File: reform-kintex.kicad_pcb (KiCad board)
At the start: 8 copper layers, 68 x 67.8 mm, 345 parts, among them J1 Conn_01x33, J2 JTAG_01x06, J3 Conn_01x03_Male, U1 MNT Reform 2.0 SoM Socket, U10 W25Q128JVS, U11 TPS62823DLC, U12 TPS62823DLC, U13 TPS62823DLC, U14 TPS62823DLC, U15 TPS62823DLC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

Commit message: more routing (39)
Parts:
- C82, C83: moved to F.Cu
- R26, R53: moved to B.Cu
- moved TP5 16.5 mm to (114.8, 147.9)
- moved C97 14.2 mm to (132.7, 105.7), turned to 180 degrees
- moved FB2 11.7 mm to (132.9, 107.0), turned to 180 degrees
- moved C93 10.2 mm to (141.7, 110.7), turned to 270 degrees
- moved FB1 9.35 mm to (143.3, 109.2), turned to 270 degrees
- moved C89 7.90 mm to (144.7, 109.8)
- moved R56 7.72 mm to (164.9, 125.5), turned to 180 degrees
- moved R50 6.37 mm to (151.2, 163.5), turned to 90 degrees
- moved C87 5.92 mm to (133.3, 102.5), turned to 180 degrees
- moved R53 5.33 mm to (161.3, 142.1), turned to 180 degrees
- moved C22 5.15 mm to (150.8, 162.0), turned to 180 degrees
- moved R51 5.06 mm to (152.8, 161.8)
- moved C94 4.97 mm to (143.4, 107.2), turned to 180 degrees
- moved C90 4.55 mm to (137.6, 102.5)
- moved C98 4.49 mm to (139.5, 105.3), turned to 0 degrees
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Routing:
- net GND: track 712.9 -> 942.5 mm, vias 287 -> 341
- net +3V3: track 227.7 -> 412.4 mm, vias 23 -> 33
- net EN_VDDR: track 0.00 -> 124.0 mm, vias 0 -> 4
- net +1V2: track 136.1 -> 257.2 mm, vias 24 -> 31
- net +5V: track 159.7 -> 198.4 mm, vias 8 -> 14
- net VTTREF: track 83.0 -> 117.2 mm, vias 10 -> 15
- net EN_VIO: track 56.5 -> 83.5 mm, vias 3 -> 4
- net +1V1: track 96.5 -> 121.6 mm, vias 26 -> 29
- net ETH_VDDL: track 0.00 -> 21.6 mm, vias 0 -> 2
- net Vtt: track 32.6 -> 53.8 mm, vias 0 -> 6
- net QSPI_DQ2: track 2.50 -> 23.4 mm, vias 1 -> 2
- net DSI_RST_N: track 2.73 -> 23.6 mm, vias 2 -> 3
- net HDMI_SDA: track 28.3 -> 48.6 mm
- net HDMI_SCL: track 28.6 -> 48.6 mm
- net EN_VAUX: track 0.00 -> 19.7 mm, vias 0 -> 2
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- added copper zone on GND2.Cu, net GND
- added copper zone on GND3.Cu, net GND

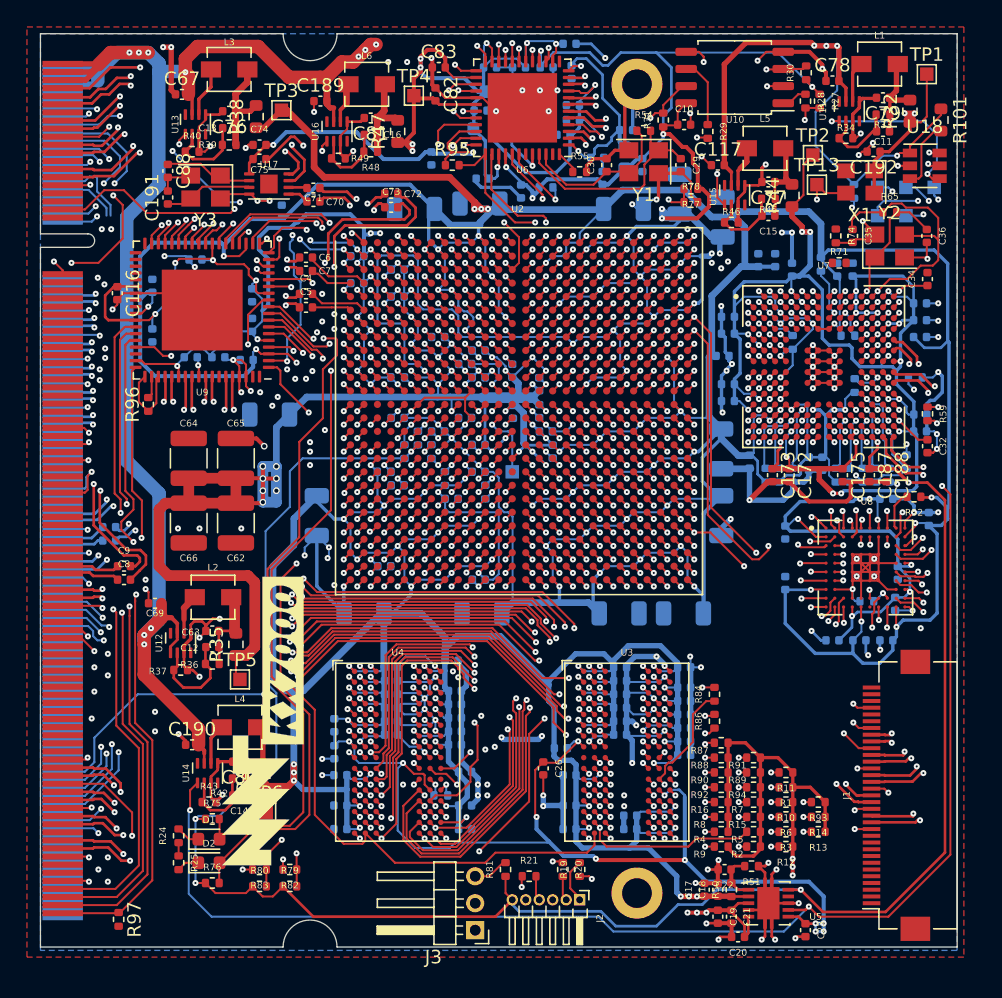
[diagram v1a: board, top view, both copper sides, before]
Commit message: fully routed
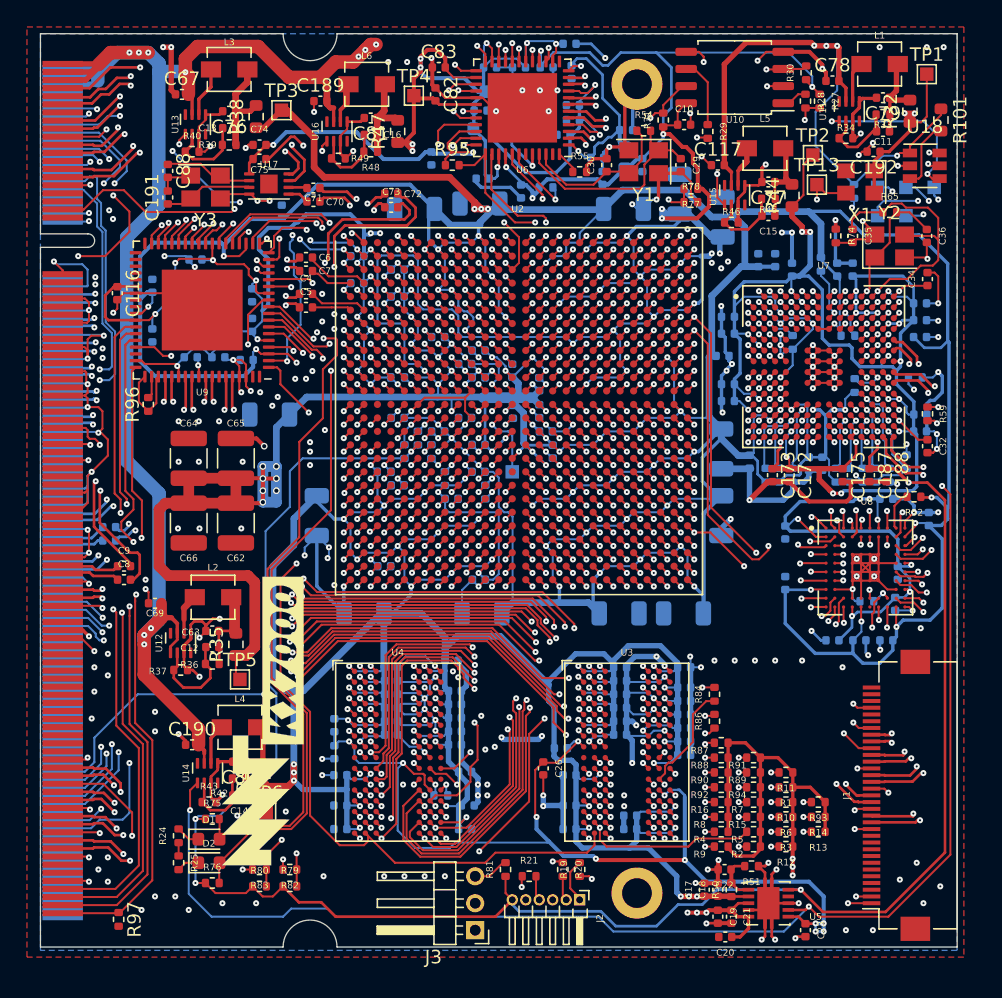
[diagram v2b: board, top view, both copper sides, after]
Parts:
- removed R71: 0, Resistor_SMD:R_0402_1005Metric
- moved C20 0.95 mm to (150.8, 167.0)
- moved C164 0.20 mm to (131.7, 157.2)
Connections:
- U1 pad 13: GND -> Net-(U1-Pad13)
- U1 pad 25: GND -> Net-(U1-Pad25)
- U2 pad G16: UART3_TX -> UART3_RX
- U2 pad H16: UART3_RX -> UART3_TX
- U2 pad Y23: Net-(U2-PadY23) -> TUSB_CLKOUT
- U7 pad D10: Net-(R71-Pad1) -> TUSB_CLKOUT
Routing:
- net GND: track 942.5 -> 1095.8 mm, vias 341 -> 380
- net TUSB_CLKOUT: track 0.00 -> 27.2 mm, vias 0 -> 2
- net UART3_RX: track 44.7 -> 57.7 mm
- net UART3_TX: track 47.1 -> 59.4 mm
- net +1V8: track 455.5 -> 460.3 mm
- net Net-(R71-Pad1): track 4.80 -> 0.00 mm, vias 1 -> 0
- net (no net): track 3.96 -> 0.00 mm, vias 7 -> 0
- net /RAM/USB2_GTX_P: track 44.0 -> 42.7 mm
- net ETH0_LED_LINK1: track 63.5 -> 64.5 mm
- net ETH0_LED_RX: track 76.1 -> 77.0 mm
- net USB2_RX_N: track 54.2 -> 53.4 mm
- net EDP_IRQ: track 2.71 -> 1.97 mm
- net EDP_RESETn: track 2.67 -> 1.97 mm
- net Net-(U2-PadY23): track 0.71 -> 0.00 mm, vias 1 -> 0
- net USB2_RX_P: track 55.9 -> 55.2 mm
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
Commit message: connect some missing i2c signals, backlight_en
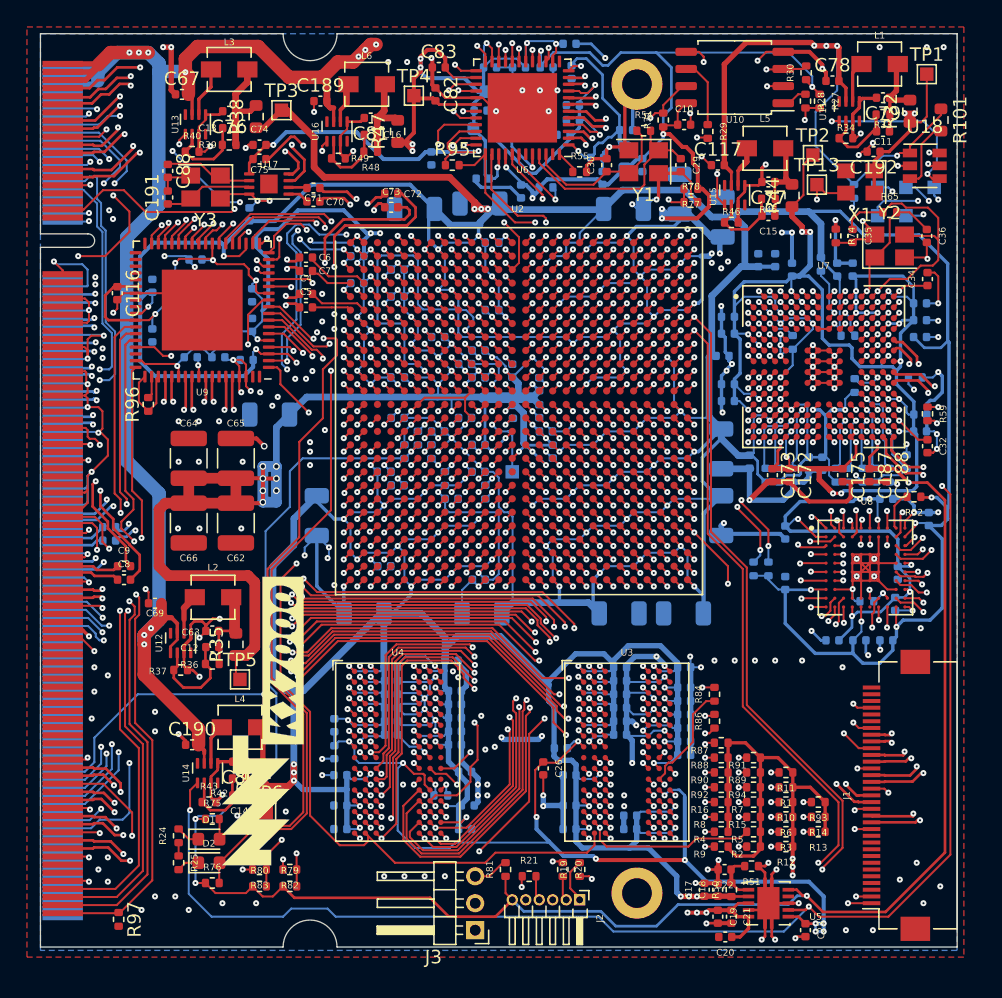
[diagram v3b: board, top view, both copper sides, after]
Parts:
- added R102: 4k7, Resistor_SMD:R_0402_1005Metric, B.Cu at (133.5, 120.5)
- added R103: 4k7, Resistor_SMD:R_0402_1005Metric, B.Cu at (154.0, 139.7)
- added R104: 4k7, Resistor_SMD:R_0402_1005Metric, B.Cu at (152.9, 139.7)
- added R71: 4k7, Resistor_SMD:R_0402_1005Metric, B.Cu at (133.5, 115.5)
- moved C118 2.41 mm to (115.5, 113.4)
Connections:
- net Net-(U8-PadK6) renamed DSI_REFCLK
- U1 pad 104: GND -> Net-(U1-Pad104)
- U2 pad B16: Net-(U2-PadB16) -> BACKLIGHT_EN
- U2 pad G26: I2C1_SCL -> DAC_SDA
- U2 pad H26: I2C1_SDA -> DAC_SCL
- U2 pad W26: Net-(U2-PadW26) -> DISP2_SDA
- U2 pad Y26: Net-(U2-PadY26) -> DISP2_SCL
- U8 pad A8: I2C1_SCL -> DISP2_SCL
- U8 pad B8: I2C1_SDA -> DISP2_SDA
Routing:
- net DAC_SDA: track 0.00 -> 124.2 mm, vias 0 -> 3
- net DAC_SCL: track 0.00 -> 121.6 mm, vias 0 -> 3
- net BACKLIGHT_EN: track 0.00 -> 55.6 mm, vias 0 -> 4
- net I2C1_SCL: track 33.4 -> 0.00 mm, vias 3 -> 0
- net I2C1_SDA: track 31.6 -> 0.00 mm, vias 3 -> 0
- net DISP2_SCL: track 0.00 -> 21.7 mm, vias 0 -> 4
- net DISP2_SDA: track 0.00 -> 20.3 mm, vias 0 -> 4
- net +1V8: track 460.3 -> 463.3 mm
- net TUSB_TX_D1: track 11.1 -> 8.20 mm
- net /RAM/PCIE2_GTX_CLK_HOST_P: track 14.2 -> 11.6 mm
- net TUSB_TX_DATAK1: track 21.2 -> 23.1 mm
- net DSI_RST_N: track 23.6 -> 25.3 mm
- net TUSB_TX_D0: track 12.8 -> 11.3 mm
- net DISP1_SDA: track 29.2 -> 30.4 mm
- net TUSB_CLKOUT: track 27.2 -> 26.1 mm
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
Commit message: silkscreen cleanup, 3d models, some footprint fixes
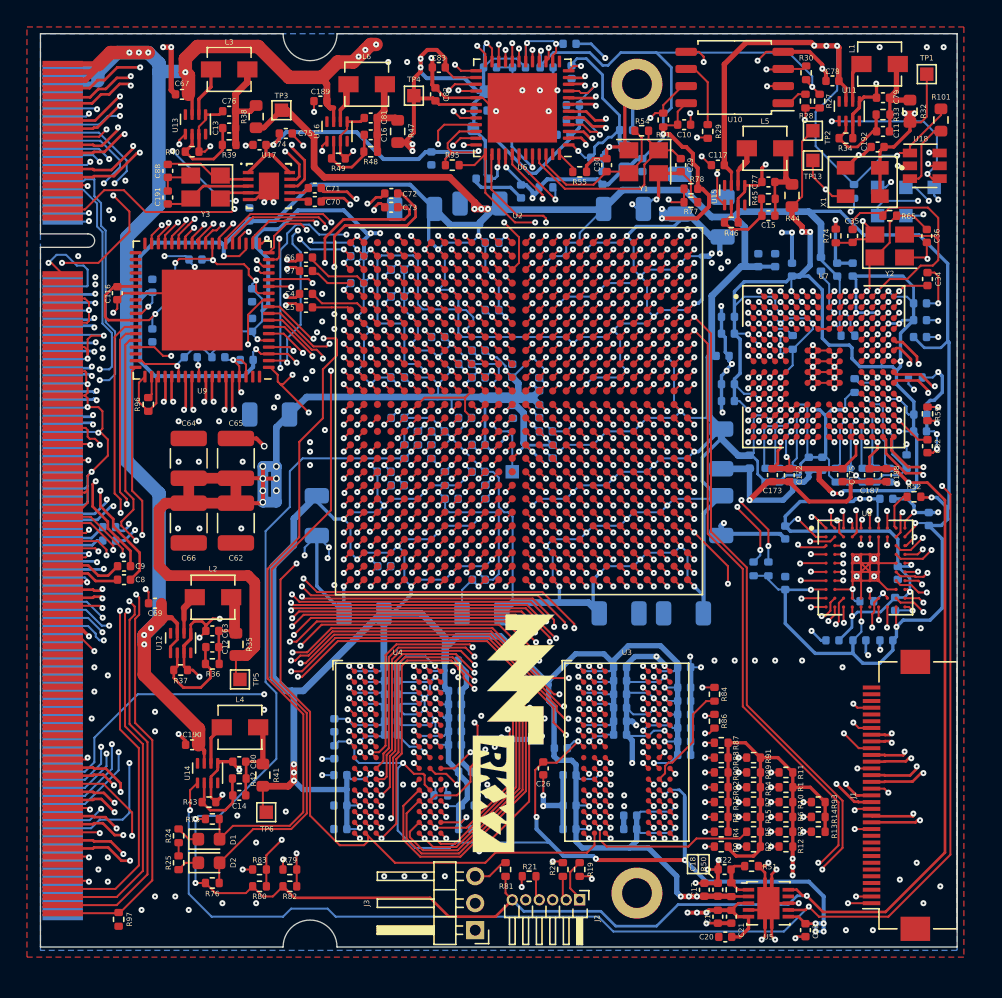
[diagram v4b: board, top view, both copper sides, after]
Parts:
- GFX1: footprint footprints:mnt-kx7000 -> footprints:mnt-rkx7
- U17: value Si52112-B6 -> Si52112-B5-GM2; footprint Package_DFN_QFN:TDFN-8-1EP_3x2mm_P0.5mm_EP1.3x1.4mm -> footprints:Silicon_Labs-Si52112-B5-GM2-Level_B
- X1: footprint Oscillator:Oscillator_SMD_Abracon_ASE-4Pin_3.2x2.5mm -> footprints:OSCDFN500X320X90-4N
- moved GFX1 18.6 mm to (135.1, 151.9), turned to 270 degrees
- moved C75 2.72 mm to (118.2, 107.4)
- moved TP13 1.82 mm to (157.3, 109.4)
- moved TP2 1.80 mm to (157.3, 107.2)
- moved C192 0.46 mm to (162.1, 108.4)
- moved R65 0.25 mm to (163.0, 113.5)
- moved X1 0.20 mm to (161.0, 111.0)
- moved R54 0.15 mm to (144.6, 107.2)
- moved U17 0.15 mm to (117.0, 111.3)
- moved C70 0.10 mm to (120.3, 112.5)
- moved C71 0.10 mm to (120.3, 111.5)
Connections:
- U1 pad 107: EDP_SCL -> DISP1_SCL
- U1 pad 109: EDP_SDA -> DISP1_SDA
- U17 pad 5: PCIE1_CLK_HOST_P -> GND
- U17 pad 6: PCIE1_CLK_HOST_N -> PCIE1_CLK_HOST_P
- U17 pad 7: PCIE1_CLK_P -> PCIE1_CLK_HOST_N
- U17 pad 8: PCIE1_CLK_N -> PCIE1_CLK_P
- U17 pad 9: (no net) -> PCIE1_CLK_N
- U2 pad C14: Net-(U2-PadC14) -> EDP_RESETn
- U2 pad D13: Net-(U2-PadD13) -> USB_RESETn
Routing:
- net USB_RESETn: track 2.75 -> 80.3 mm, vias 1 -> 2
- net EDP_RESETn: track 1.97 -> 44.5 mm, vias 1 -> 3
- net DISP1_SCL: track 25.9 -> 52.1 mm, vias 2 -> 4
- net DISP1_SDA: track 30.4 -> 55.3 mm, vias 3 -> 4
- net +3V3: track 413.8 -> 417.2 mm
- net USB2_RX_P: track 55.0 -> 52.3 mm
- net GND: track 1095.1 -> 1097.5 mm, vias 375 -> 371
- net USB2_RX_N: track 53.3 -> 50.8 mm
- net +1V1: track 121.6 -> 123.4 mm
- net BACKLIGHT_EN: track 55.6 -> 53.9 mm
- net SD2_CMD: track 45.9 -> 47.4 mm
- net CLK_100MHZ: track 24.1 -> 25.5 mm
- net DAC_SDA: track 124.2 -> 123.3 mm
- net SD2_DATA3: track 46.4 -> 47.3 mm
- net HDMI_SDA: track 48.3 -> 49.1 mm
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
